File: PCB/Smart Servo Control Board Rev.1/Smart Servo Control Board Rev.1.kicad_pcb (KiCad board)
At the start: 4 copper layers, 36.8 x 16.5 mm, 38 parts, among them J1 PRGR, J2 CTRL, J3 CTRL, J4 MOT, J5 MOT, Q1 AO3400A, Q2 AO3400A, U1 AMS1117-3.3, U2 STM32F030C8Tx, U3 INA219AxD, U4 INA219AxD, U5 IRF7307, U6 AS5600, U7 IRF7307

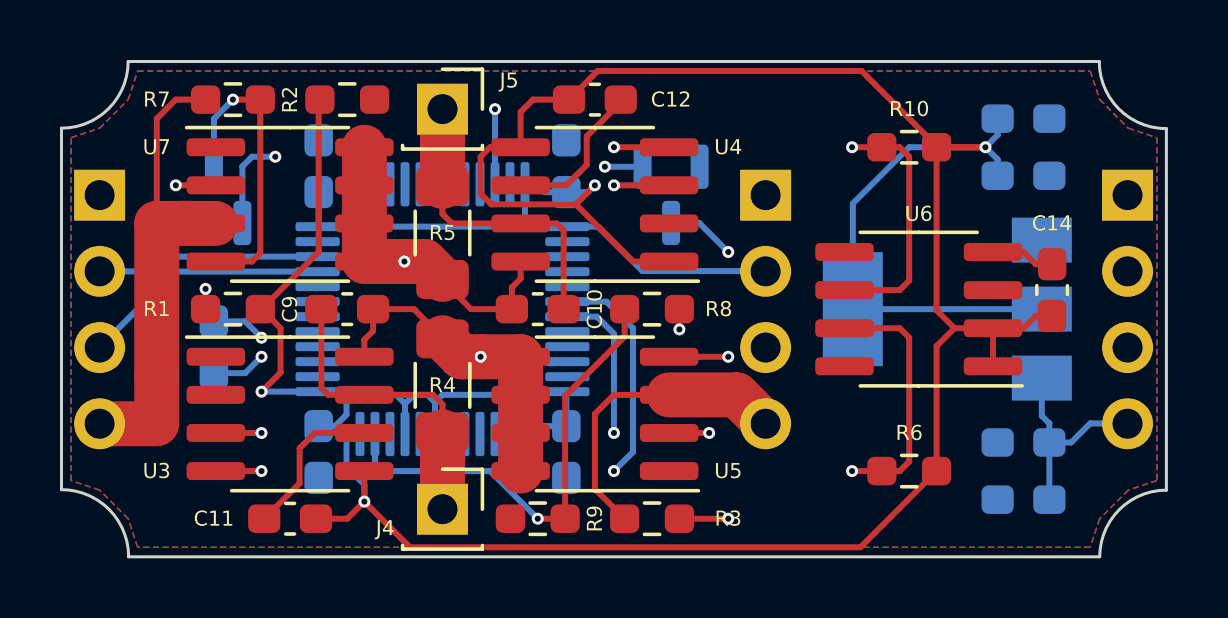
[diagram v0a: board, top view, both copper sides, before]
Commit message: Aggiunti datasheet componenti e aggiunta EEPROM
aggiunto chip EEPROMi2c e datasheet per INA219 e 24LC256.
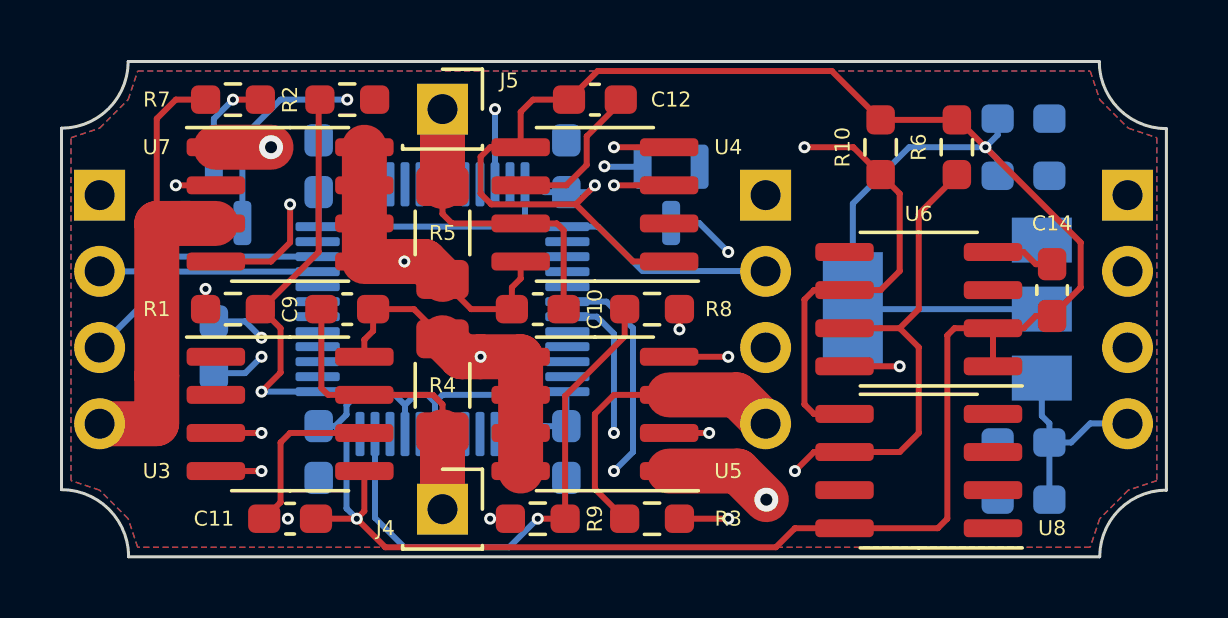
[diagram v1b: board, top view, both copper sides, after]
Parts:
- added U8: 24LC256, Package_SO:SOIC-8_3.9x4.9mm_P1.27mm, F.Cu at (99.7, 41.6)
- moved R6 10.9 mm to (101.0, 30.8), turned to 90 degrees
- moved R10 0.95 mm to (98.4, 30.8), turned to 90 degrees
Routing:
- net GNDD: track 12.5 -> 20.3 mm, vias 0 -> 5
- net SCL1: track 50.4 -> 56.2 mm
- net SDA1: track 45.4 -> 50.3 mm
- net Net-(Q2-Pad3): track 10.1 -> 12.6 mm, vias 1 -> 2
- net B': track 28.9 -> 30.8 mm
- net B: track 15.9 -> 17.7 mm
- net +3V3: track 115.9 -> 117.2 mm
